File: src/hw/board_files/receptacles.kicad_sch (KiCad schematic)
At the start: 14 parts, among them J2 USB_A, J4 USB_C_Receptacle_USB2.0_14P, J6 Micro_SD_Card_Det1, U8 USB2244-AEZG-06, Y2 24MHz

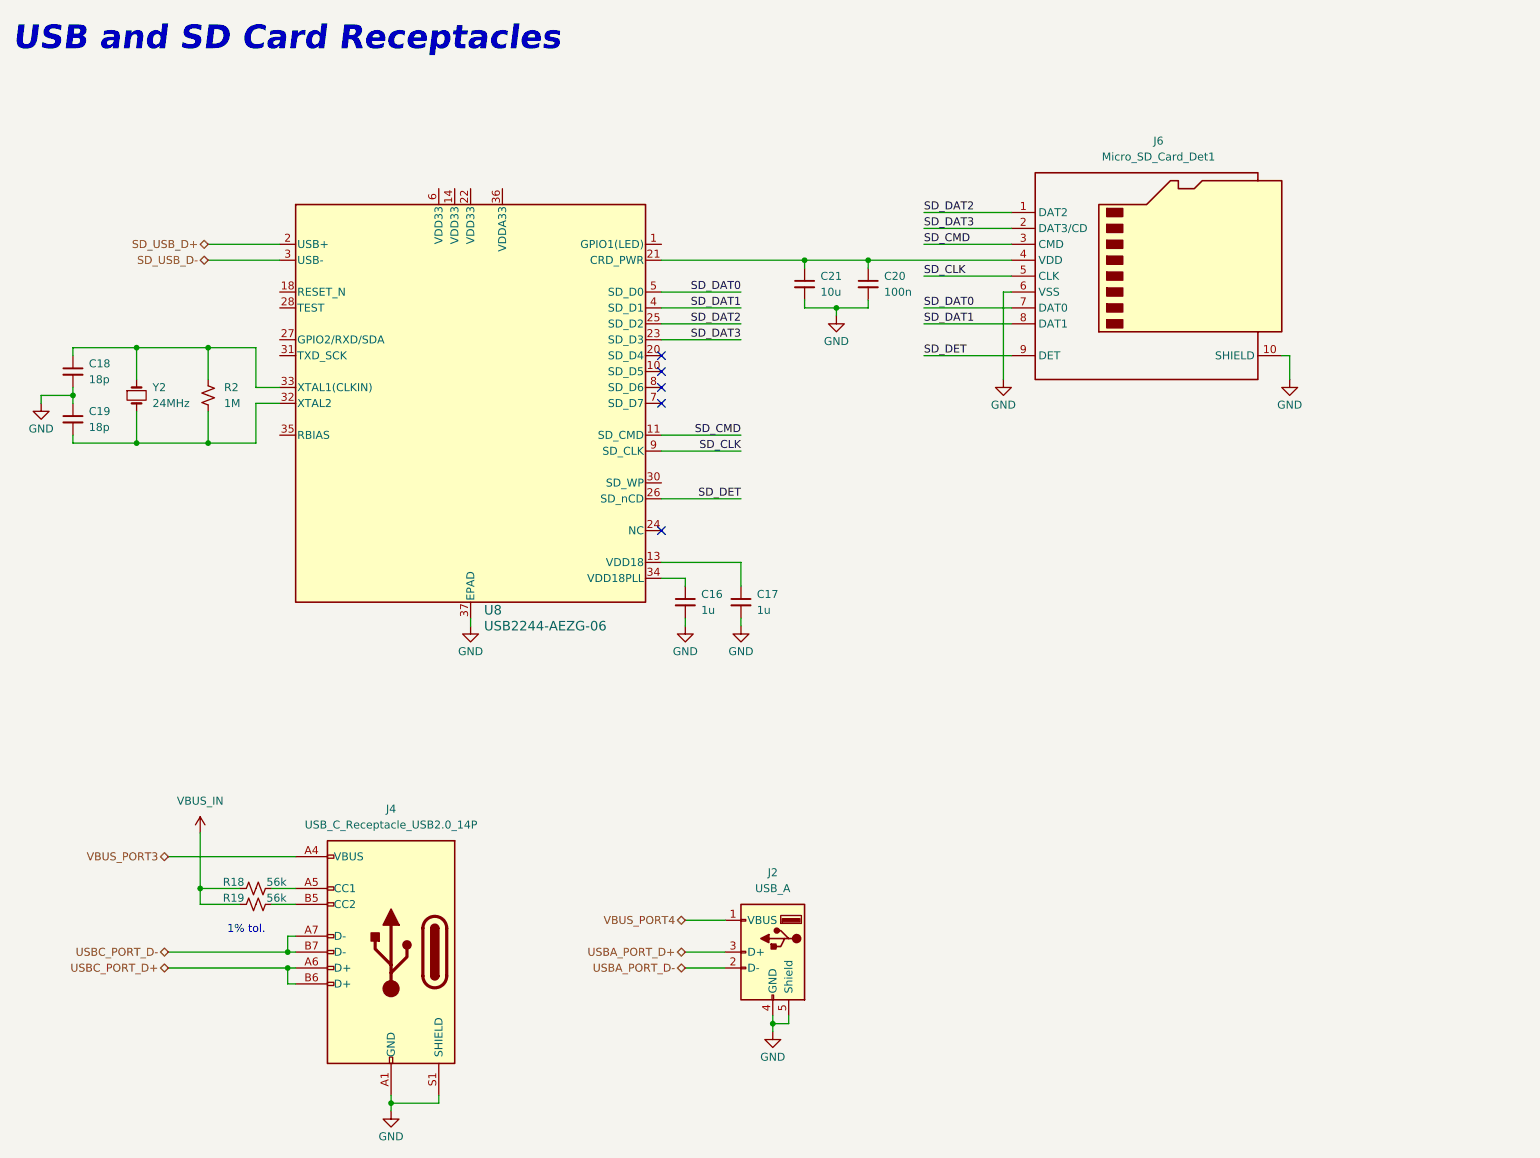
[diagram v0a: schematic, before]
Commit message: Finishing schematic. Need to review and clean up
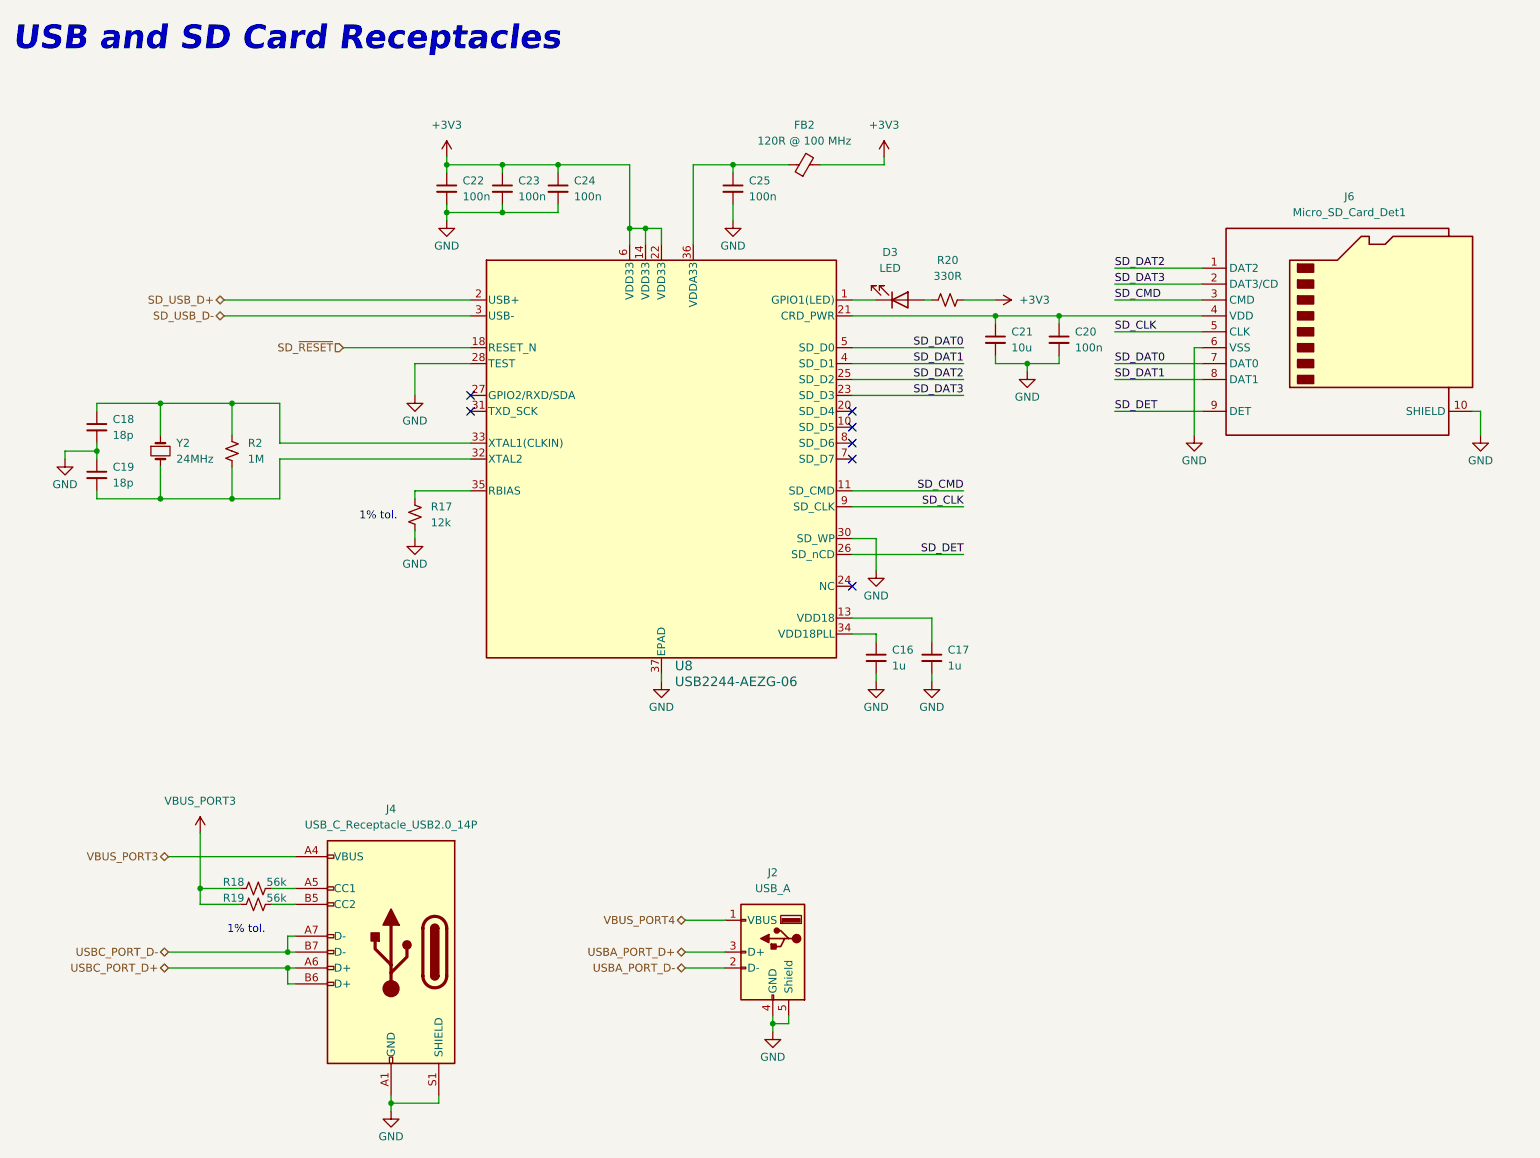
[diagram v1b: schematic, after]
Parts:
- added C22, C23, C24, C25: 100n, symbol Device:C_Small
- added D3: LED, symbol Device:LED
- added FB2: 120R @ 100 MHz, symbol Device:FerriteBead_Small
- added R17: 12k, symbol Device:R_Small_US
- added R20: 330R, symbol Device:R_Small_US
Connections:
- net VBUS_IN is gone; now on net VBUS_PORT3: R18.2, R19.2
- net GND: now also U8.28 (TEST), U8.30 (SD_WP), C22.2, C23.2, C24.2, C25.2, R17.2
- net at U8.1 (GPIO1(LED)): now also D3.1 (K)
- net +3V3: now reaches U8.14 (VDD33)
- net +3V3: now also U8.22 (VDD33), U8.6 (VDD33), C22.1, C23.1, C24.1, FB2.2, R20.2
- net SD_~{RESET}: now reaches U8.18 (RESET_N)
- net at U8.35 (RBIAS): now also R17.1
- net at U8.36 (VDDA33): now also C25.1, FB2.1
- new net: D3.2 (A), R20.1
- no-connect marks 5 -> 7
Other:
- moved on the sheet: C16, C17, C18, C19, C20, C21, J6, R2, U8, Y2

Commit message: Added all footprints, need to connect switches to MCU
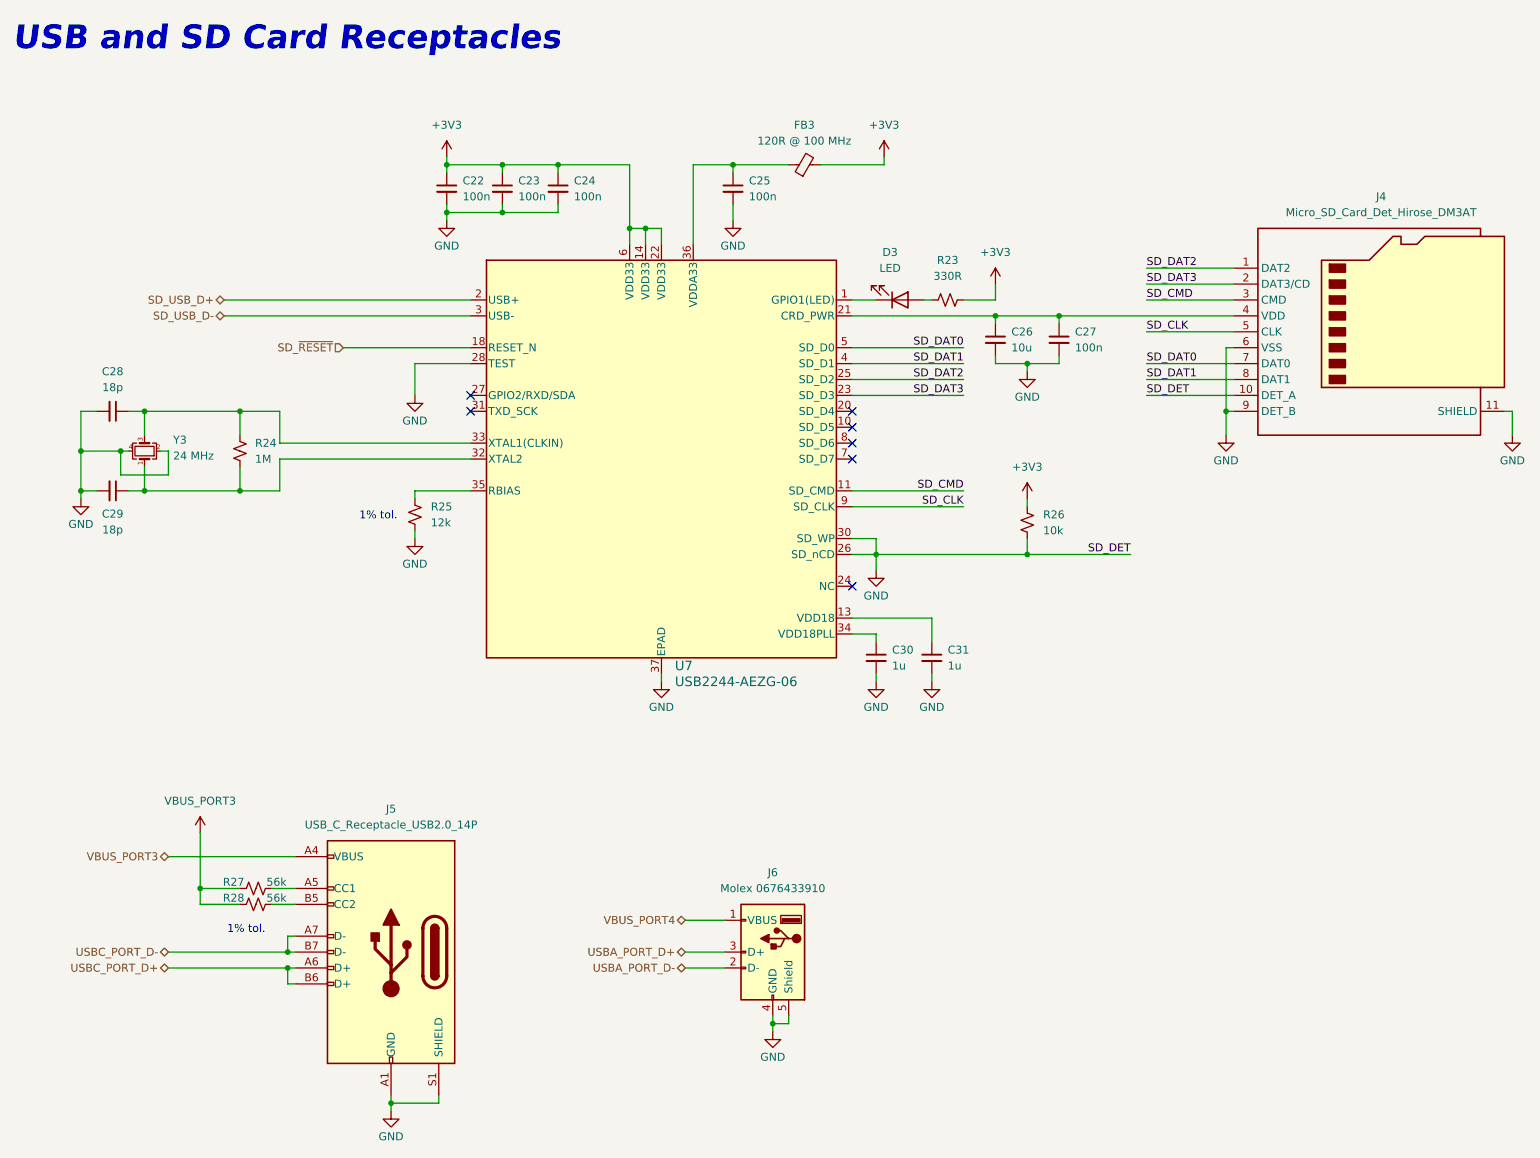
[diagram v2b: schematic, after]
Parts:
- removed J6: Micro_SD_Card_Det1, symbol Connector:Micro_SD_Card_Det1
- removed Y2: 24MHz, symbol Device:Crystal_Small
- added J4: Micro_SD_Card_Det_Hirose_DM3AT, symbol Connector:Micro_SD_Card_Det_Hirose_DM3AT
- added R26: 10k, Resistor_SMD:R_0805_2012Metric_Pad1.20x1.40mm_HandSolder, symbol Device:R_Small_US
- added Y3: 24 MHz, Crystal:Crystal_SMD_Abracon_ABM8G-4Pin_3.2x2.5mm, symbol Device:Crystal_GND24_Small
- C22, C23, C24, C25: footprint (none) -> Capacitor_SMD:C_0603_1608Metric_Pad1.08x0.95mm_HandSolder
- C26: renamed from C21; footprint (none) -> Capacitor_SMD:C_0805_2012Metric_Pad1.18x1.45mm_HandSolder
- C27: renamed from C20; footprint (none) -> Capacitor_SMD:C_0603_1608Metric_Pad1.08x0.95mm_HandSolder
- C28: renamed from C18; footprint (none) -> Capacitor_SMD:C_0603_1608Metric_Pad1.08x0.95mm_HandSolder
- C29: renamed from C19; footprint (none) -> Capacitor_SMD:C_0603_1608Metric_Pad1.08x0.95mm_HandSolder
- C30: renamed from C16; footprint (none) -> Capacitor_SMD:C_0603_1608Metric_Pad1.08x0.95mm_HandSolder
- C31: renamed from C17; footprint (none) -> Capacitor_SMD:C_0603_1608Metric_Pad1.08x0.95mm_HandSolder
- D3: footprint (none) -> LED_SMD:LED_0603_1608Metric_Pad1.05x0.95mm_HandSolder
- FB3: renamed from FB2; footprint (none) -> Inductor_SMD:L_0603_1608Metric_Pad1.05x0.95mm_HandSolder
- J6: renamed from J2; value USB_A -> Molex 0676433910; footprint (none) -> Connector_USB:USB_A_Molex_67643_Horizontal
- R23: renamed from R20; footprint (none) -> Resistor_SMD:R_0805_2012Metric_Pad1.20x1.40mm_HandSolder
- R24: renamed from R2; footprint (none) -> Resistor_SMD:R_0603_1608Metric_Pad0.98x0.95mm_HandSolder
- R25: renamed from R17; footprint (none) -> Resistor_SMD:R_0805_2012Metric_Pad1.20x1.40mm_HandSolder
- R27: renamed from R18; footprint (none) -> Resistor_SMD:R_0805_2012Metric_Pad1.20x1.40mm_HandSolder
- R28: renamed from R19; footprint (none) -> Resistor_SMD:R_0805_2012Metric_Pad1.20x1.40mm_HandSolder
- renumbered J4 to J5, U8 to U7
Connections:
- net SD_DET is gone; now on net GND: U7.26 (SD_nCD)
- net +3V3: now also R26.2
- net GND: now also C29.2, J4.10 (DET_A), J4.11 (SHIELD), J4.6 (VSS), J4.9 (DET_B), R26.1, Y3.2, Y3.4; no longer C29.1
- net SD_CLK: now also J4.5 (CLK)
- net SD_CMD: now also J4.3 (CMD)
- net SD_DAT0: now also J4.7 (DAT0)
- net SD_DAT1: now also J4.8 (DAT1)
- net SD_DAT2: now also J4.1 (DAT2)
- net SD_DAT3: now also J4.2 (DAT3/CD)
- net at R24.2, U7.32 (XTAL2): now also C29.1, Y3.1; no longer C29.2
- net at C28.1, R24.1, U7.33 (XTAL1(CLKIN)): now also Y3.3
- net at C26.1, C27.1, U7.21 (CRD_PWR): now also J4.4 (VDD)
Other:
- moved on the sheet: C28, C29, R24

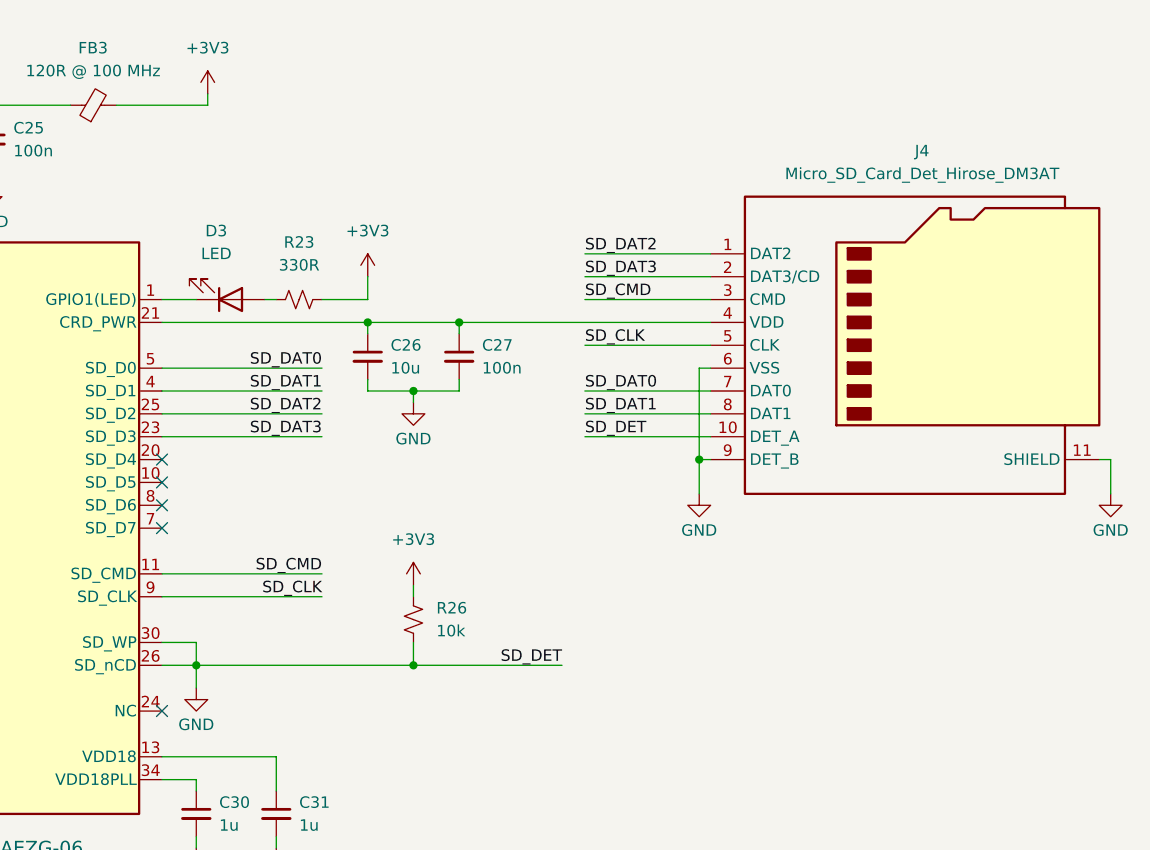
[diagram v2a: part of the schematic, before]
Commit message: Added rotary encoder and OLED. Started laying out board then I need to review schematic and change pinout if needed
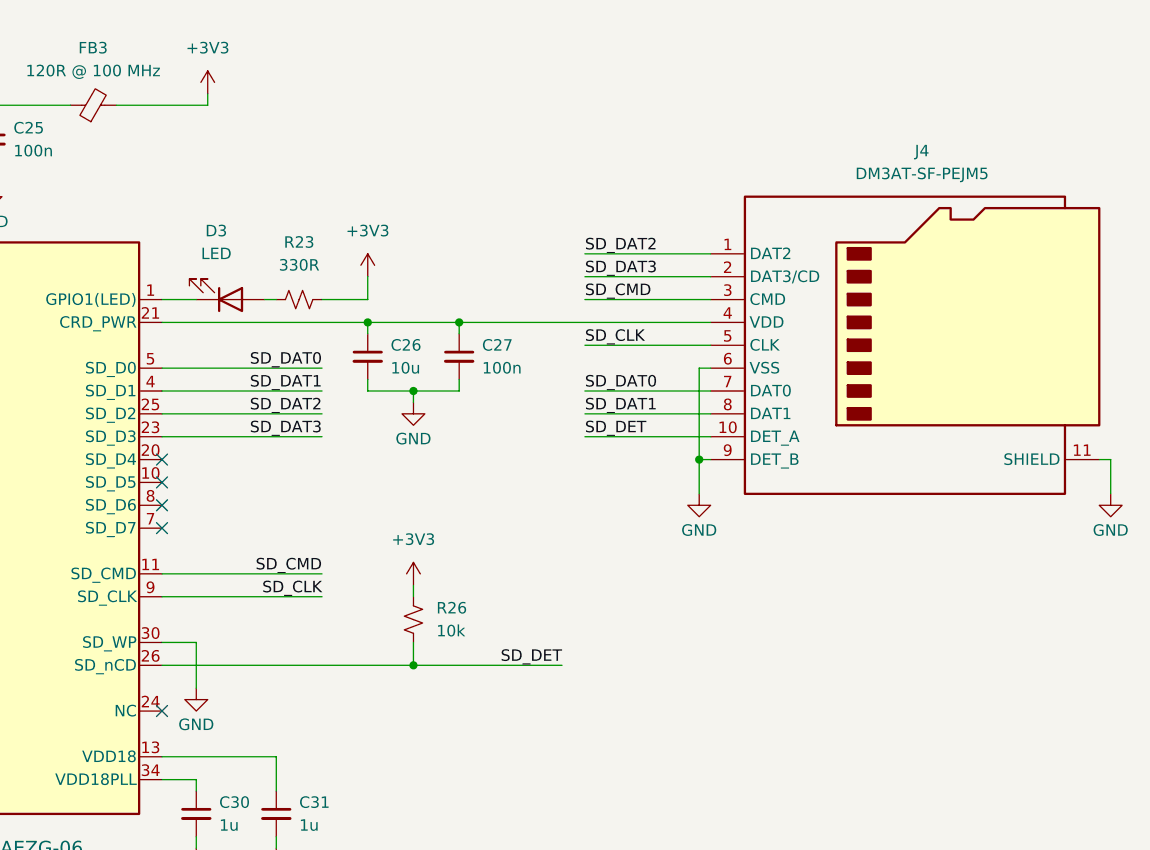
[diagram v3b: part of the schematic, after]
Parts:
- J4: value Micro_SD_Card_Det_Hirose_DM3AT -> DM3AT-SF-PEJM5; footprint (none) -> Connector_Card:microSD_HC_Hirose_DM3AT-SF-PEJM5
- R23, R25, R26, R27, R28: footprint Resistor_SMD:R_0805_2012Metric_Pad1.20x1.40mm_HandSolder -> Resistor_SMD:R_0603_1608Metric_Pad0.98x0.95mm_HandSolder
- R24: footprint Resistor_SMD:R_0603_1608Metric_Pad0.98x0.95mm_HandSolder -> Resistor_SMD:R_0805_2012Metric_Pad1.20x1.40mm_HandSolder
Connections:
- net GND: no longer J4.10 (DET_A), R26.1, U7.26 (SD_nCD)
- new net SD_DET: J4.10 (DET_A), R26.1, U7.26 (SD_nCD)
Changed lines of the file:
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@@
 	)
 	(junction
-		(at 151.13 99.06)
-		(diameter 0)
-		(color 0 0 0 0)
-	)
-	(junction
 		(at 100.33 36.83)
 		(diameter 0)
@@
 	)
 	(junction
-		(at 175.26 99.06)
-		(diameter 0)
-		(color 0 0 0 0)
-	)
-	(junction
 		(at 43.18 152.4)
 		(diameter 0)
@@
 	)
 	(junction
+		(at 175.26 99.06)
+		(diameter 0)
+		(color 0 0 0 0)
+	)
+	(junction
 		(at 34.29 76.2)
 		(diameter 0)
@@
 	(wire
 		(pts
-			(xy 151.13 99.06) (xy 151.13 101.6)
-		)
-		(stroke
-			(width 0)
-			(type default)
-		)
-	)
-	(wire
-		(pts
 			(xy 73.66 185.42) (xy 73.66 186.69)
 		)
@@
 	(wire
 		(pts
-			(xy 151.13 96.52) (xy 151.13 99.06)
+			(xy 151.13 96.52) (xy 151.13 101.6)
 		)
 		(stroke
@@
 	(wire
 		(pts
+			(xy 147.32 99.06) (xy 175.26 99.06)
+		)
+		(stroke
+			(width 0)
+			(type default)
+		)
+	)
+	(wire
+		(pts
 			(xy 170.18 60.96) (xy 180.34 60.96)
 		)
@@
 	(wire
 		(pts
-			(xy 151.13 99.06) (xy 147.32 99.06)
-		)
-		(stroke
-			(width 0)
-			(type default)
-		)
-	)
-	(wire
-		(pts
 			(xy 121.92 36.83) (xy 121.92 49.53)
 		)
@@
 	(wire
 		(pts
-			(xy 151.13 99.06) (xy 175.26 99.06)
-		)
-		(stroke
-			(width 0)
-			(type default)
-		)
-	)
-	(wire
-		(pts
 			(xy 91.44 44.45) (xy 82.55 44.45)
 		)
@@
 			)
 		)
-		(property "Footprint" "Resistor_SMD:R_0805_2012Metric_Pad1.20x1.40mm_HandSolder"
+		(property "Footprint" "Resistor_SMD:R_0603_1608Metric_Pad0.98x0.95mm_HandSolder"
 			(at 52.07 154.94 0)
 			(effects
@@
 			)
 		)
-		(property "Footprint" "Resistor_SMD:R_0805_2012Metric_Pad1.20x1.40mm_HandSolder"
+		(property "Footprint" "Resistor_SMD:R_0603_1608Metric_Pad0.98x0.95mm_HandSolder"
 			(at 77.47 92.71 0)
 			(effects
@@
 			)
 		)
-		(property "Footprint" "Resistor_SMD:R_0805_2012Metric_Pad1.20x1.40mm_HandSolder"
+		(property "Footprint" "Resistor_SMD:R_0603_1608Metric_Pad0.98x0.95mm_HandSolder"
 			(at 162.56 58.42 0)
 			(effects
@@
 			)
 		)
-		(property "Footprint" "Resistor_SMD:R_0805_2012Metric_Pad1.20x1.40mm_HandSolder"
+		(property "Footprint" "Resistor_SMD:R_0603_1608Metric_Pad0.98x0.95mm_HandSolder"
 			(at 52.07 152.4 0)
 			(effects
@@
 			)
 		)
-		(property "Footprint" "Resistor_SMD:R_0603_1608Metric_Pad0.98x0.95mm_HandSolder"
+		(property "Footprint" "Resistor_SMD:R_0805_2012Metric_Pad1.20x1.40mm_HandSolder"
 			(at 49.53 82.55 0)
 			(effects
@@
 			)
 		)
-		(property "Value" "Micro_SD_Card_Det_Hirose_DM3AT"
+		(property "Value" "DM3AT-SF-PEJM5"
 			(at 231.775 44.45 0)
 			(effects
@@
 			)
 		)
-		(property "Footprint" ""
+		(property "Footprint" "Connector_Card:microSD_HC_Hirose_DM3AT-SF-PEJM5"
 			(at 283.21 45.72 0)
 			(effects
@@
 			)
 		)
-		(property "Datasheet" "https://www.hirose.com/product/en/download_file/key_name/DM3/category/Catalog/doc_file_id/49662/?file_category_id=4&item_id=195&is_series=1"
+		(property "Datasheet" "https://www.hirose.com/product/document?clcode=CL0609-0033-6-00&productname=DM3AT-SF-PEJ2M5&series=DM3&documenttype=Catalog&lang=en&documentid=D49662_en"
 			(at 231.14 60.96 0)
 			(effects
@@
 			)
 		)
-		(property "Footprint" "Resistor_SMD:R_0805_2012Metric_Pad1.20x1.40mm_HandSolder"
+		(property "Footprint" "Resistor_SMD:R_0603_1608Metric_Pad0.98x0.95mm_HandSolder"
 			(at 175.26 93.98 0)
 			(effects
